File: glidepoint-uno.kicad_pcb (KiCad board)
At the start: 2 copper layers, 68.6 x 53.3 mm, 13 parts, among them J1 Power, J2 Digital/PWM, J3 Analog, J4 Digital/PWM, J5 Conn_01x12_Socket, SW1 SW_Push, SW2 SW_Push

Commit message: Routing tweaks.
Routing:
- net +3V3: track 54.1 -> 64.7 mm
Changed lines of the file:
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@@
     )
   )
+  (property "SHA1" "21dd6ff")
+  (property "TIMESTAMP" "2023-06-20")
   (net 0 "")
   (net 1 "GND")
@@
   (segment (start 102.04 88.055) (end 102.04 89.54) (width 0.25) (layer "B.Cu") (net 14))
   (segment (start 102.04 89.54) (end 102.68 90.18) (width 0.25) (layer "B.Cu") (net 14))
-  (segment (start 117.56 93.79) (end 131.89 93.79) (width 0.25) (layer "B.Cu") (net 16))
-  (segment (start 131.89 93.79) (end 135.56 97.46) (width 0.25) (layer "B.Cu") (net 16))
-  (segment (start 109.215 79.705) (end 114.095 84.585) (width 0.25) (layer "B.Cu") (net 16))
+  (segment (start 100.415 70.605) (end 100.38 70.64) (width 0.25) (layer "B.Cu") (net 16))
+  (segment (start 133.62 99.4) (end 135.56 97.46) (width 0.25) (layer "B.Cu") (net 16))
+  (segment (start 102.11 99.4) (end 133.62 99.4) (width 0.25) (layer "B.Cu") (net 16))
   (segment (start 101.33 70.605) (end 100.415 70.605) (width 0.25) (layer "B.Cu") (net 16))
-  (segment (start 100.38 70.64) (end 100.38 76.61) (width 0.25) (layer "B.Cu") (net 16))
-  (segment (start 114.095 90.325) (end 117.56 93.79) (width 0.25) (layer "B.Cu") (net 16))
-  (segment (start 114.095 84.585) (end 114.095 90.325) (width 0.25) (layer "B.Cu") (net 16))
-  (segment (start 100.38 76.61) (end 103.475 79.705) (width 0.25) (layer "B.Cu") (net 16))
-  (segment (start 100.415 70.605) (end 100.38 70.64) (width 0.25) (layer "B.Cu") (net 16))
-  (segment (start 103.475 79.705) (end 109.215 79.705) (width 0.25) (layer "B.Cu") (net 16))
+  (segment (start 100.38 97.67) (end 102.11 99.4) (width 0.25) (layer "B.Cu") (net 16))
+  (segment (start 100.38 70.64) (end 100.38 97.67) (width 0.25) (layer "B.Cu") (net 16))
   (segment (start 107.163832 72.105) (end 101.33 72.105) (width 0.25) (layer "B.Cu") (net 21))
   (segment (start 119.78 50.184) (end 119.78 59.488832) (width 0.25) (layer "B.Cu") (net 21))

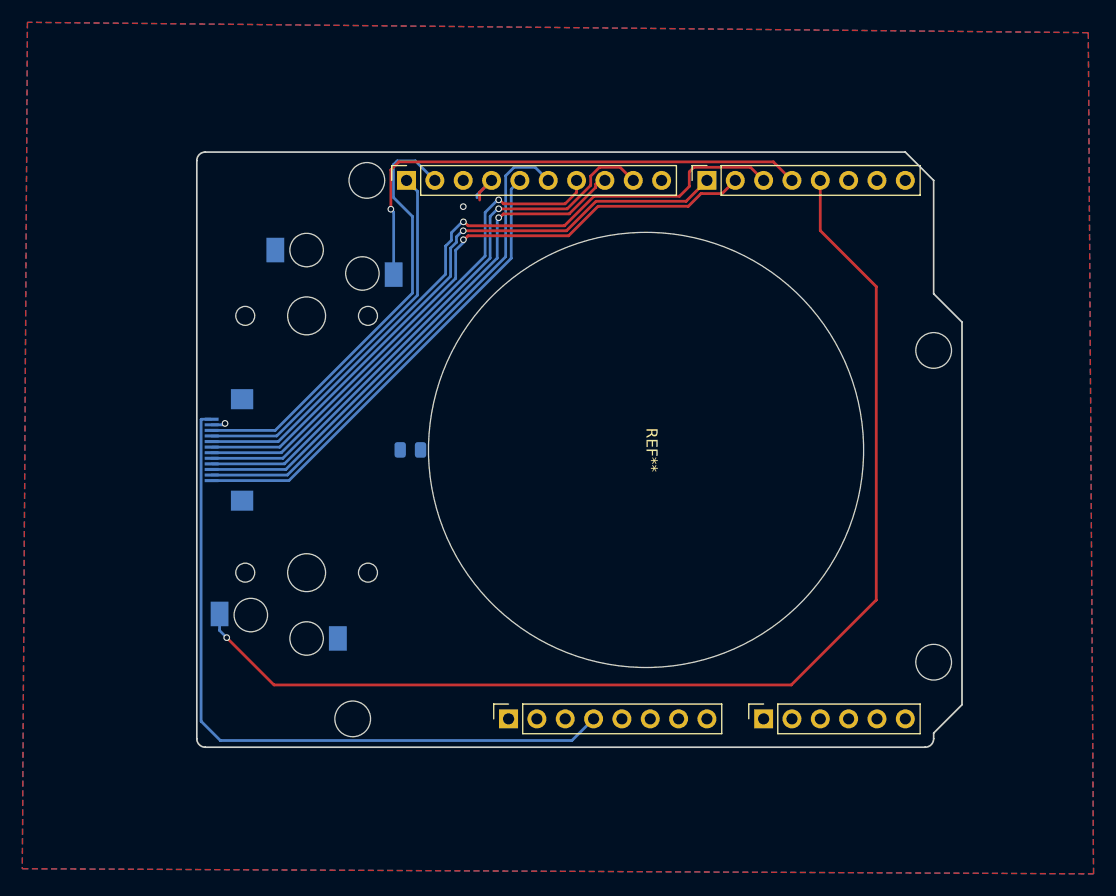
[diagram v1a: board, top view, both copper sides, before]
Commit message: Add 3 mounting holes.
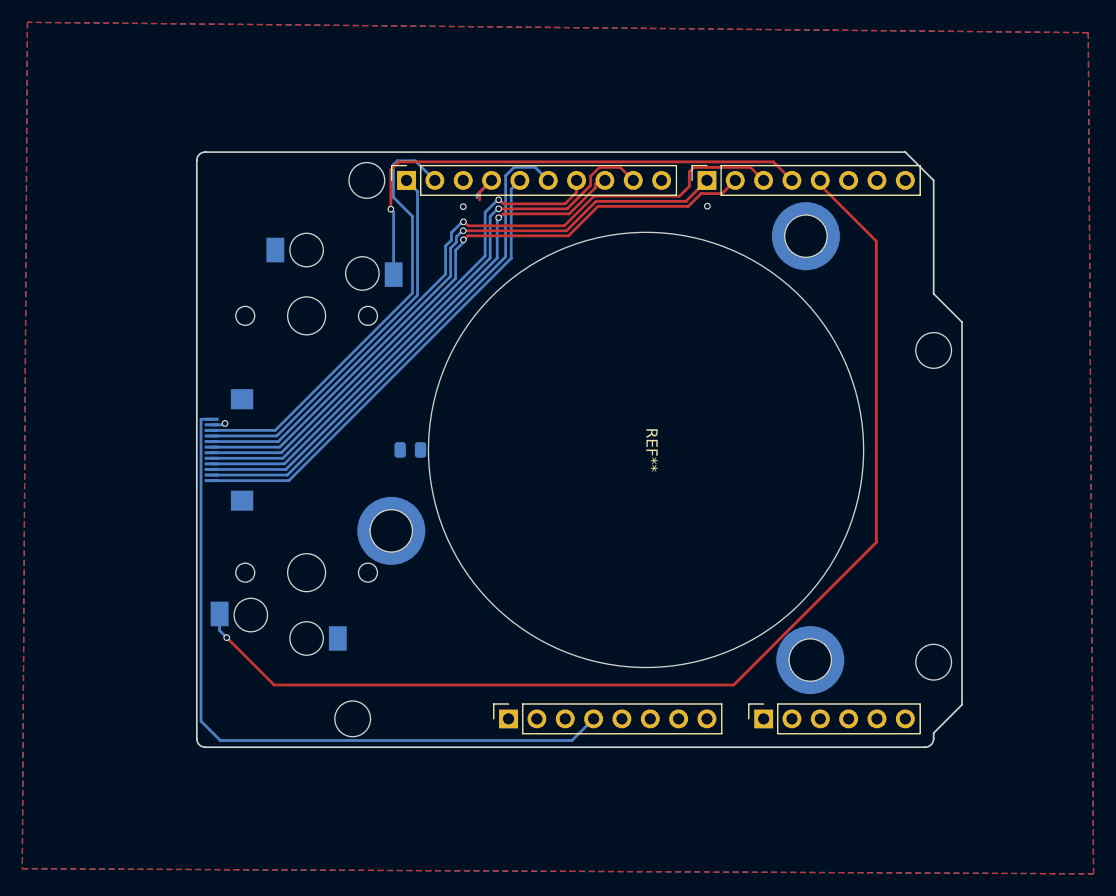
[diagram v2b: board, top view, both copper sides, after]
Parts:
- added H1: MountingHole, mounting:MountingHole_M2_Pad_NonPTH_TopOnly, B.Cu at (117.4, 80.6)
- added H2: MountingHole, mounting:MountingHole_M2_Pad_NonPTH_TopOnly, B.Cu at (155.0, 92.2)
- added H3: MountingHole, mounting:MountingHole_M2_Pad_NonPTH_TopOnly, B.Cu at (154.6, 54.2)
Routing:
- net SW2: track 105.2 -> 102.2 mm
- net GND: vias 2 -> 3
